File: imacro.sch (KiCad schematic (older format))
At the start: 28 parts, among them SW0:0 Choc, SW0:1 Choc, SW0:2 Choc, SW1 TOGGLE, SW1:0 Choc, SW1:1 Choc, SW1:2 Choc, SW2:0 Choc, SW2:1 Choc, SW2:2 Choc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

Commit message: add footprint for kailh pg1350 switch
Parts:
- SW0:0, SW0:1, SW0:2, SW1:0, SW1:1, SW1:2, SW2:0, SW2:1, SW2:2, SW3:0, SW3:1, SW3:2: footprint (none) -> imacro:PG1350
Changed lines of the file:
@@
 F 0 "SW3:0" H 6200 2200 50  0000 L CNN
 F 1 "Choc" H 6150 2040 50  0000 C CNN
-F 2 "" H 6150 2300 50  0001 C CNN
+F 2 "imacro:PG1350" H 6150 2300 50  0001 C CNN
 F 3 "" H 6150 2300 50  0001 C CNN
 	1    6150 2100
@@
 F 0 "SW3:1" H 6900 2200 50  0000 L CNN
 F 1 "Choc" H 6850 2040 50  0000 C CNN
-F 2 "" H 6850 2300 50  0001 C CNN
+F 2 "imacro:PG1350" H 6850 2300 50  0001 C CNN
 F 3 "" H 6850 2300 50  0001 C CNN
 	1    6850 2100
@@
 F 0 "SW3:2" H 7600 2200 50  0000 L CNN
 F 1 "Choc" H 7550 2040 50  0000 C CNN
-F 2 "" H 7550 2300 50  0001 C CNN
+F 2 "imacro:PG1350" H 7550 2300 50  0001 C CNN
 F 3 "" H 7550 2300 50  0001 C CNN
 	1    7550 2100
@@
 F 0 "SW2:0" H 6200 2900 50  0000 L CNN
 F 1 "Choc" H 6150 2740 50  0000 C CNN
-F 2 "" H 6150 3000 50  0001 C CNN
+F 2 "imacro:PG1350" H 6150 3000 50  0001 C CNN
 F 3 "" H 6150 3000 50  0001 C CNN
 	1    6150 2800
@@
 F 0 "SW2:1" H 6900 2900 50  0000 L CNN
 F 1 "Choc" H 6850 2740 50  0000 C CNN
-F 2 "" H 6850 3000 50  0001 C CNN
+F 2 "imacro:PG1350" H 6850 3000 50  0001 C CNN
 F 3 "" H 6850 3000 50  0001 C CNN
 	1    6850 2800
@@
 F 0 "SW2:2" H 7600 2900 50  0000 L CNN
 F 1 "Choc" H 7550 2740 50  0000 C CNN
-F 2 "" H 7550 3000 50  0001 C CNN
+F 2 "imacro:PG1350" H 7550 3000 50  0001 C CNN
 F 3 "" H 7550 3000 50  0001 C CNN
 	1    7550 2800
@@
 F 0 "SW1:0" H 6200 3600 50  0000 L CNN
 F 1 "Choc" H 6150 3440 50  0000 C CNN
-F 2 "" H 6150 3700 50  0001 C CNN
+F 2 "imacro:PG1350" H 6150 3700 50  0001 C CNN
 F 3 "" H 6150 3700 50  0001 C CNN
 	1    6150 3500
@@
 F 0 "SW1:1" H 6900 3600 50  0000 L CNN
 F 1 "Choc" H 6850 3440 50  0000 C CNN
-F 2 "" H 6850 3700 50  0001 C CNN
+F 2 "imacro:PG1350" H 6850 3700 50  0001 C CNN
 F 3 "" H 6850 3700 50  0001 C CNN
 	1    6850 3500
@@
 F 0 "SW1:2" H 7600 3600 50  0000 L CNN
 F 1 "Choc" H 7550 3440 50  0000 C CNN
-F 2 "" H 7550 3700 50  0001 C CNN
+F 2 "imacro:PG1350" H 7550 3700 50  0001 C CNN
 F 3 "" H 7550 3700 50  0001 C CNN
 	1    7550 3500
@@
 F 0 "SW0:0" H 6200 4300 50  0000 L CNN
 F 1 "Choc" H 6150 4140 50  0000 C CNN
-F 2 "" H 6150 4400 50  0001 C CNN
+F 2 "imacro:PG1350" H 6150 4400 50  0001 C CNN
 F 3 "" H 6150 4400 50  0001 C CNN
 	1    6150 4200
@@
 F 0 "SW0:1" H 6900 4300 50  0000 L CNN
 F 1 "Choc" H 6850 4140 50  0000 C CNN
-F 2 "" H 6850 4400 50  0001 C CNN
+F 2 "imacro:PG1350" H 6850 4400 50  0001 C CNN
 F 3 "" H 6850 4400 50  0001 C CNN
 	1    6850 4200
@@
 F 0 "SW0:2" H 7600 4300 50  0000 L CNN
 F 1 "Choc" H 7550 4140 50  0000 C CNN
-F 2 "" H 7550 4400 50  0001 C CNN
+F 2 "imacro:PG1350" H 7550 4400 50  0001 C CNN
 F 3 "" H 7550 4400 50  0001 C CNN
 	1    7550 4200

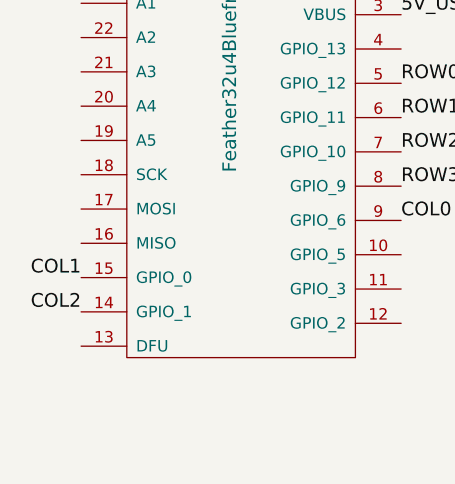
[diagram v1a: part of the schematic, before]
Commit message: create board layout
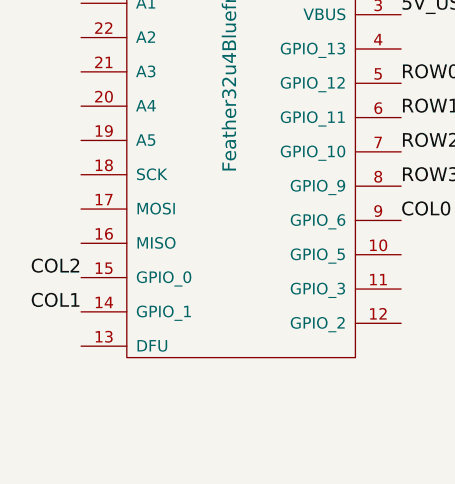
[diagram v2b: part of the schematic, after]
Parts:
- QI1: footprint Wire_Pads:SolderWirePad_2x_2-5mmDrill -> imacro:QI_connector
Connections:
- net COL1: now also U1.14 (GPIO_1); no longer U1.15 (GPIO_0)
- net COL2: now also U1.15 (GPIO_0); no longer U1.14 (GPIO_1)
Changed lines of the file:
@@
 Text Label 3075 3925 0    60   ~ 0
 COL0
+Text Label 1675 4325 2    60   ~ 0
+COL1
 Text Label 1675 4175 2    60   ~ 0
-COL1
-Text Label 1675 4325 2    60   ~ 0
 COL2
 $Comp
@@
 F 0 "QI1" H 2375 1150 50  0000 L CNN
 F 1 "QI_Receiver" H 2375 1050 50  0000 L CNN
-F 2 "Wire_Pads:SolderWirePad_2x_2-5mmDrill" V 2275 1110 50  0001 C CNN
+F 2 "imacro:QI_connector" V 2275 1110 50  0001 C CNN
 F 3 "" V 2275 1110 50  0001 C CNN
 	1    2275 1050

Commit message: Finish PCB layout; add necessary footprints to library; adjust pad drill size for key switches
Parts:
- SW1: footprint (none) -> imacro:GPTS_SPST_Pushbutton
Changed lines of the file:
@@
 F 0 "SW1" H 3450 2650 50  0000 C CNN
 F 1 "TOGGLE" H 3450 2425 50  0000 C CNN
-F 2 "" H 3450 2525 50  0001 C CNN
+F 2 "imacro:GPTS_SPST_Pushbutton" H 3450 2525 50  0001 C CNN
 F 3 "" H 3450 2525 50  0001 C CNN
 	1    3450 2525

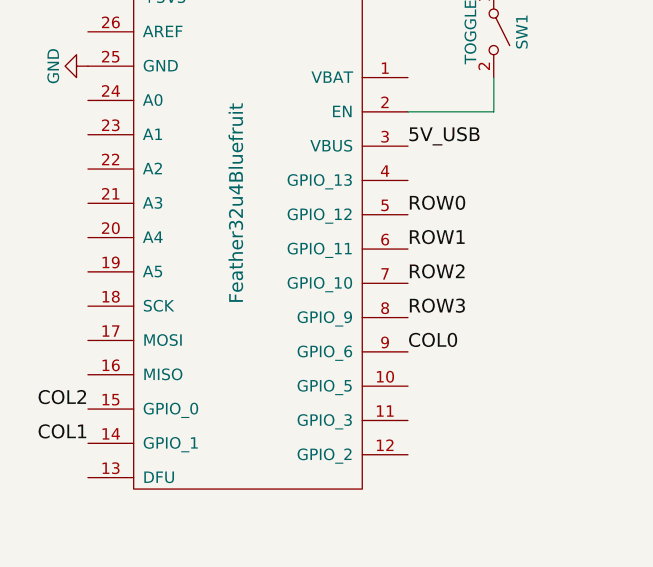
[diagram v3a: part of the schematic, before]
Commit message: Don’t use pin 9 on the feather so it can be used to read the battery level
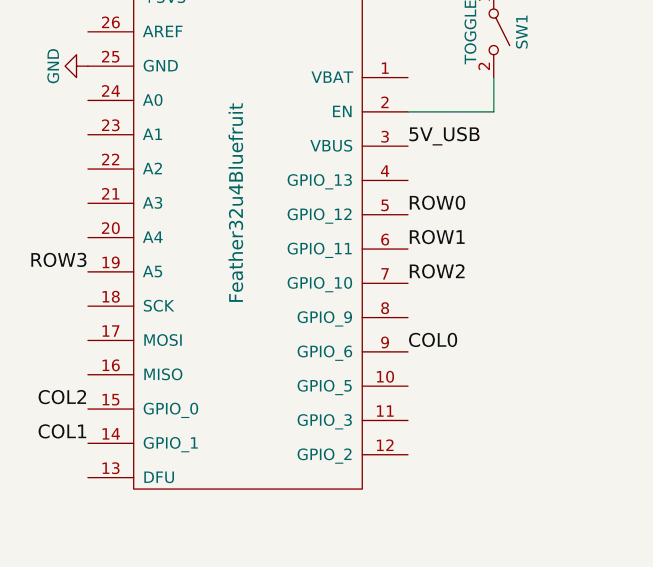
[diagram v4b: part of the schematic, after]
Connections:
- net ROW3: now also U1.19 (A5); no longer U1.8 (GPIO_9)
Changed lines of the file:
@@
 Text Label 3075 3625 0    60   ~ 0
 ROW2
-Text Label 3075 3775 0    60   ~ 0
+Text Label 1675 3575 2    60   ~ 0
 ROW3
 Text Label 3075 3925 0    60   ~ 0

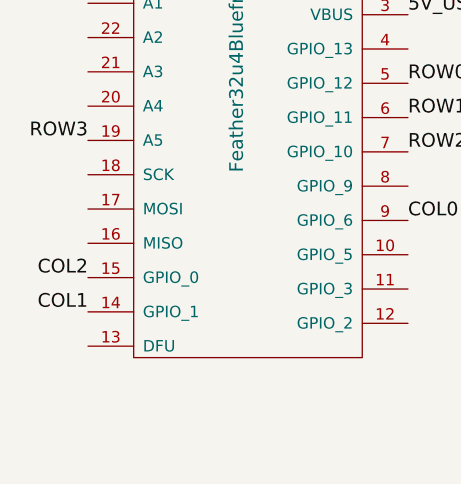
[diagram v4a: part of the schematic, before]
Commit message: accomodate smaller case; rotate Feather board around for new battery cable position; improve trace routing somewhat
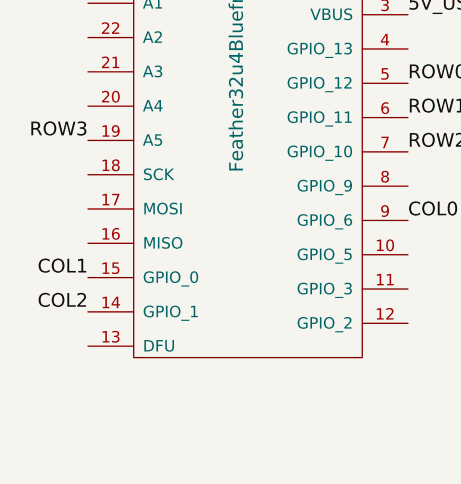
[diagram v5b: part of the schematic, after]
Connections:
- net COL1: now also U1.15 (GPIO_0); no longer U1.14 (GPIO_1)
- net COL2: now also U1.14 (GPIO_1); no longer U1.15 (GPIO_0)
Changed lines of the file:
@@
 Text Label 3075 3925 0    60   ~ 0
 COL0
+Text Label 1675 4175 2    60   ~ 0
+COL1
 Text Label 1675 4325 2    60   ~ 0
-COL1
-Text Label 1675 4175 2    60   ~ 0
 COL2
 $Comp
